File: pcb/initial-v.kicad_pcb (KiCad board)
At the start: 2 copper layers, 28.9 x 59.5 mm, 30 parts, among them J1 USB_C_Receptacle_USB2.0, J2 Barrel_Jack_Switch_Pin3Ring, J3 Conn_01x10, Q1 MBT3904DW1, SW1 SW_SPST, SW2 SW_SPST, U1 MCP2221AxSL, U2 MCP1700-1202E_SOT89, U3 ESP32-MINI-1-H4, U4 MPM3610GQV-Z, U5 SN65HVD230

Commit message: updating design
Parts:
- added D1: 12v, LED_SMD:LED_1206_3216Metric_Pad1.42x1.75mm_HandSolder, F.Cu at (143.6, 98.7)
- added D2: 5v, LED_SMD:LED_1206_3216Metric_Pad1.42x1.75mm_HandSolder, F.Cu at (118.6, 102.7)
- added D3: 3v, LED_SMD:LED_1206_3216Metric_Pad1.42x1.75mm_HandSolder, F.Cu at (141.4, 89.7)
- added G***: LOGO, artwork:mise, B.Cu at (112.3, 83.0)
- added R11: 100k, Resistor_SMD:R_1206_3216Metric_Pad1.30x1.75mm_HandSolder, F.Cu at (134.9, 105.1)
- added R12: 1k, Resistor_SMD:R_1206_3216Metric_Pad1.30x1.75mm_HandSolder, F.Cu at (147.5, 98.7)
- added R13: 100, Resistor_SMD:R_1206_3216Metric_Pad1.30x1.75mm_HandSolder, F.Cu at (125.0, 102.7)
- added R14: 100, Resistor_SMD:R_1206_3216Metric_Pad1.30x1.75mm_HandSolder, F.Cu at (141.4, 92.9)
- moved R10 29.9 mm to (113.1, 72.4)
- moved J1 28.7 mm to (110.8, 105.9)
- moved R2 27.9 mm to (114.1, 86.3)
- moved R9 26.0 mm to (118.7, 76.9), turned to -90 degrees
- moved R5 24.4 mm to (111.5, 102.7), turned to 180 degrees
- moved R4 23.8 mm to (121.2, 107.3), turned to 90 degrees
- moved R3 23.3 mm to (121.9, 86.3), turned to -90 degrees
- moved C1 23.0 mm to (111.8, 97.1), turned to -90 degrees
- moved U5 22.6 mm to (112.9, 78.2), turned to 90 degrees
- moved U1 22.3 mm to (118.0, 94.9), turned to 180 degrees
- moved R1 20.9 mm to (124.1, 97.0), turned to 90 degrees
- moved Q1 20.5 mm to (118.0, 87.0)
- moved R7 18.8 mm to (139.6, 98.6), turned to -90 degrees
- moved J2 18.5 mm to (142.5, 104.0)
- moved C8 17.3 mm to (130.9, 105.1), turned to 90 degrees
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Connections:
- C2 pad 1: Net-(C2-Pad1) -> +3V3
- C3 pad 1: Net-(C2-Pad1) -> +3V3
- R6 pad 1: Net-(C2-Pad1) -> +3V3
- U3 pad 3: Net-(C2-Pad1) -> +3V3
- U4 pad 17: +12V -> Net-(U4-Pad17)
- U4 pad 3: unconnected-(U4-Pad3) -> GND
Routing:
- net +3V3: track 45.1 -> 94.7 mm, vias 3 -> 4
- net Net-(C2-Pad1): track 30.2 -> 0.00 mm, vias 2 -> 0
- net +12V: track 67.3 -> 86.9 mm, vias 1 -> 0
- net /CAN_RX: track 39.0 -> 22.0 mm
- net /D-: track 28.3 -> 12.7 mm, vias 1 -> 0
- net /D+: track 29.8 -> 14.3 mm
- net Net-(R1-Pad2): track 18.8 -> 3.89 mm
- net /GP0: track 9.08 -> 21.4 mm
- net /CAN_LOW: track 45.3 -> 35.9 mm
- net /RX: track 18.9 -> 28.2 mm
- net /ESP_RST: track 73.2 -> 81.2 mm
- net Net-(J1-PadB5): track 14.8 -> 7.59 mm, vias 1 -> 0
- net /CAN_HIGH: track 42.3 -> 36.3 mm
- net Net-(J1-PadA5): track 8.53 -> 3.41 mm
- net Net-(C1-Pad1): track 8.75 -> 3.95 mm
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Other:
- board size 28.9 x 59.5 mm -> 40.5 x 60 mm
- board text added: "BOOT"

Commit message: hopefully fixed the power supply issues
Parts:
- added D4: D_Schottky, Diode_SMD:D_1206_3216Metric_Pad1.42x1.75mm_HandSolder, F.Cu at (132.7, 109.9)
- added G***: LOGO, artwork:v-logo, F.Cu at (115.0, 65.9)
- C1: value 47nf -> 0.47uF
- C2: value 10uf -> 22uf
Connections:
- R1 pad 1: +5V -> +3V3
- U1 pad 1: +5V -> +3V3
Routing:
- net +3V3: track 94.7 -> 113.9 mm, vias 4 -> 6
- net +5V: track 30.6 -> 28.4 mm
- net GND: track 22.7 -> 22.6 mm, vias 12 -> 15
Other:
- board text added: "+"
- board text added: "V3"

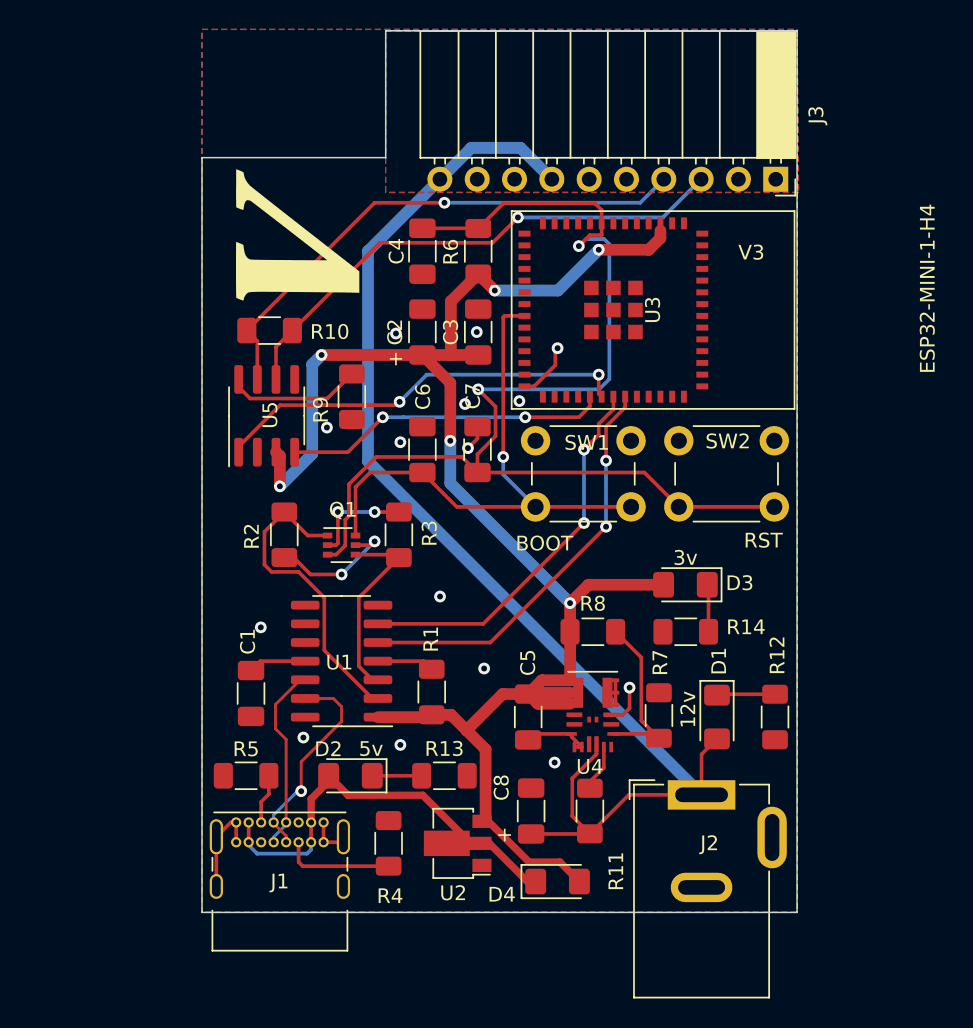
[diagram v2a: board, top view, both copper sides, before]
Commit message: I think there was a problem with the pinout in the ESP footprint
This should fix the ESP footprint
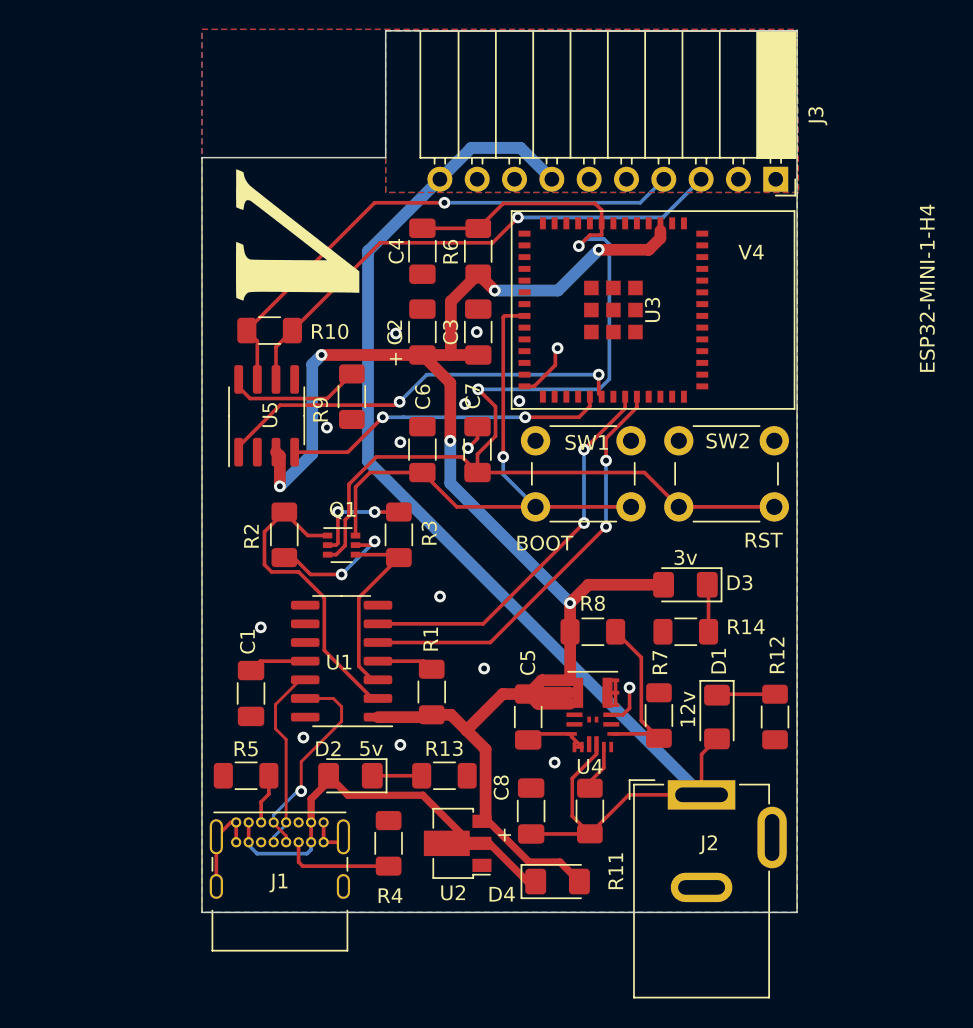
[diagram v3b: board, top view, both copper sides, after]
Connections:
- U3 pad 34: /TX -> unconnected-(U3-Pad34)
- U3 pad 35: /RX -> /TX
- U3 pad 36: unconnected-(U3-Pad36) -> /RX
- U3 pad 37: GND -> unconnected-(U3-Pad37)
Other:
- board text added: "V4"
- board text removed: "V3"

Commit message: update pcb
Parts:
- removed C1: 0.47uF, Capacitor_SMD:C_1206_3216Metric_Pad1.33x1.80mm_HandSolder
- removed D2: 5v, LED_SMD:LED_1206_3216Metric_Pad1.42x1.75mm_HandSolder
- removed the G*** at (115.0, 65.9)
- removed Q1: MBT3904DW1, Package_TO_SOT_SMD:SOT-363_SC-70-6
- removed R1, R2, R3: 10k, Resistor_SMD:R_1206_3216Metric_Pad1.30x1.75mm_HandSolder
- removed R13: 100, Resistor_SMD:R_1206_3216Metric_Pad1.30x1.75mm_HandSolder
- removed R4, R5: 5.1k, Resistor_SMD:R_1206_3216Metric_Pad1.30x1.75mm_HandSolder
- removed U1: MCP2221AxSL, Package_SO:SOIC-14_3.9x8.7mm_P1.27mm
- added G***: LOGO, artwork:mise, F.Cu at (112.3, 85.9)
- J1: value USB_C_Receptacle_USB2.0 -> Prog; footprint Connector_USB:USB_C_Receptacle_GCT_USB4085 -> Connector_PinHeader_2.54mm:PinHeader_1x04_P2.54mm_Horizontal
- J2: value Barrel_Jack_Switch_Pin3Ring -> PWR; footprint Connector_BarrelJack:BarrelJack_GCT_DCJ200-10-A_Horizontal -> Connector_PinHeader_2.54mm:PinHeader_1x03_P2.54mm_Vertical
- moved J1 32.4 mm to (138.6, 89.2)
- moved D4 17.7 mm to (129.5, 92.5), turned to 90 degrees
- moved R10 17.7 mm to (123.8, 86.4)
- moved U5 17.3 mm to (123.7, 91.6)
- moved U2 16.9 mm to (134.0, 92.5)
- moved R8 14.9 mm to (121.5, 99.0), turned to 90 degrees
- moved R9 13.5 mm to (119.5, 90.4)
- moved R14 11.5 mm to (140.9, 104.4)
- moved D3 10.8 mm to (140.9, 100.5)
- moved R7 10.1 mm to (129.5, 99.0), turned to 90 degrees
- moved R11 7.95 mm to (127.0, 106.0), turned to 90 degrees
- moved C8 7.78 mm to (123.2, 106.0), turned to -90 degrees
- moved U4 5.92 mm to (133.5, 104.0), turned to 90 degrees
- moved R12 5.77 mm to (146.4, 104.4), turned to 0 degrees
- moved C5 5.21 mm to (125.5, 99.0)
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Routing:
- net /ESP_RST: track 81.0 -> 53.5 mm
- net +12V: track 86.9 -> 112.7 mm, vias 0 -> 1
- net /CAN_LOW: track 35.9 -> 61.4 mm, vias 1 -> 0
- net /GP0: track 21.4 -> 0.00 mm
- net Net-(R7-Pad2): track 11.7 -> 32.2 mm
- net +5V: track 28.4 -> 11.8 mm
- net /D+: track 14.3 -> 0.00 mm, vias 1 -> 0
- net /GP1: track 13.2 -> 0.00 mm
- net /D-: track 12.7 -> 0.00 mm
- net /CAN_HIGH: track 36.3 -> 46.6 mm, vias 1 -> 0
- net GND: track 22.6 -> 12.4 mm, vias 15 -> 7
- net /RX: track 28.5 -> 18.8 mm, vias 2 -> 1
- net /GPIO0: track 38.7 -> 29.3 mm, vias 1 -> 0
- net Net-(Q1-Pad5): track 8.96 -> 0.00 mm, vias 2 -> 0
- net +3V3: track 113.9 -> 105.0 mm
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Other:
- board size 40.5 x 60 mm -> 40.5 x 58 mm
- board text added: "+5"
- board text added: "12v"
- board text added: "2022-12-26"
- board text added: "GND"
- board text added: "RX"
- board text added: "TX"
- board text added: "V5"
- board text removed: "V4"

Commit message: updating schematic
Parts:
- D1, D3: footprint LED_SMD:LED_1206_3216Metric_Pad1.42x1.75mm_HandSolder -> LED_SMD:LED_1206_3216Metric
- J2: value PWR -> PJ-032A; footprint Connector_PinHeader_2.54mm:PinHeader_1x03_P2.54mm_Vertical -> PJ-032A:CUI_PJ-032A
- R12, R14: footprint Resistor_SMD:R_1206_3216Metric_Pad1.30x1.75mm_HandSolder -> Resistor_SMD:R_1206_3216Metric
- moved R12 37.0 mm to (118.5, 80.0)
- moved D1 36.7 mm to (118.5, 76.5)
- moved R14 28.7 mm to (118.5, 86.5)
- moved D3 28.4 mm to (118.5, 83.0)
- moved J2 4.72 mm to (142.0, 103.0)
- moved J1 0.50 mm to (138.6, 88.7)
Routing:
- net +3V3: track 105.0 -> 112.5 mm, vias 6 -> 7
- net +12V: track 112.7 -> 119.5 mm, vias 1 -> 2
- net GND: vias 7 -> 8
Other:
- board text added: "2022-12-31"
- board text added: "V6"
- board text removed: "2022-12-26"
- board text removed: "V5"
